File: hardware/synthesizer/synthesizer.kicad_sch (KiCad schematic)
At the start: 23 parts, among them J1 USB_C_Receptacle_USB2.0_14P, J2 Conn_Coaxial, J3 Conn_Coaxial, J4 Conn_Coaxial, J5 Conn_Coaxial, J6 Conn_ARM_JTAG_SWD_10, J7 RJ45_Abracon_ARJP11A-MASA-B-A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, U1 STM32H723VGTx, U2 AP2112K-3.3, U3 USBLC6-2P6

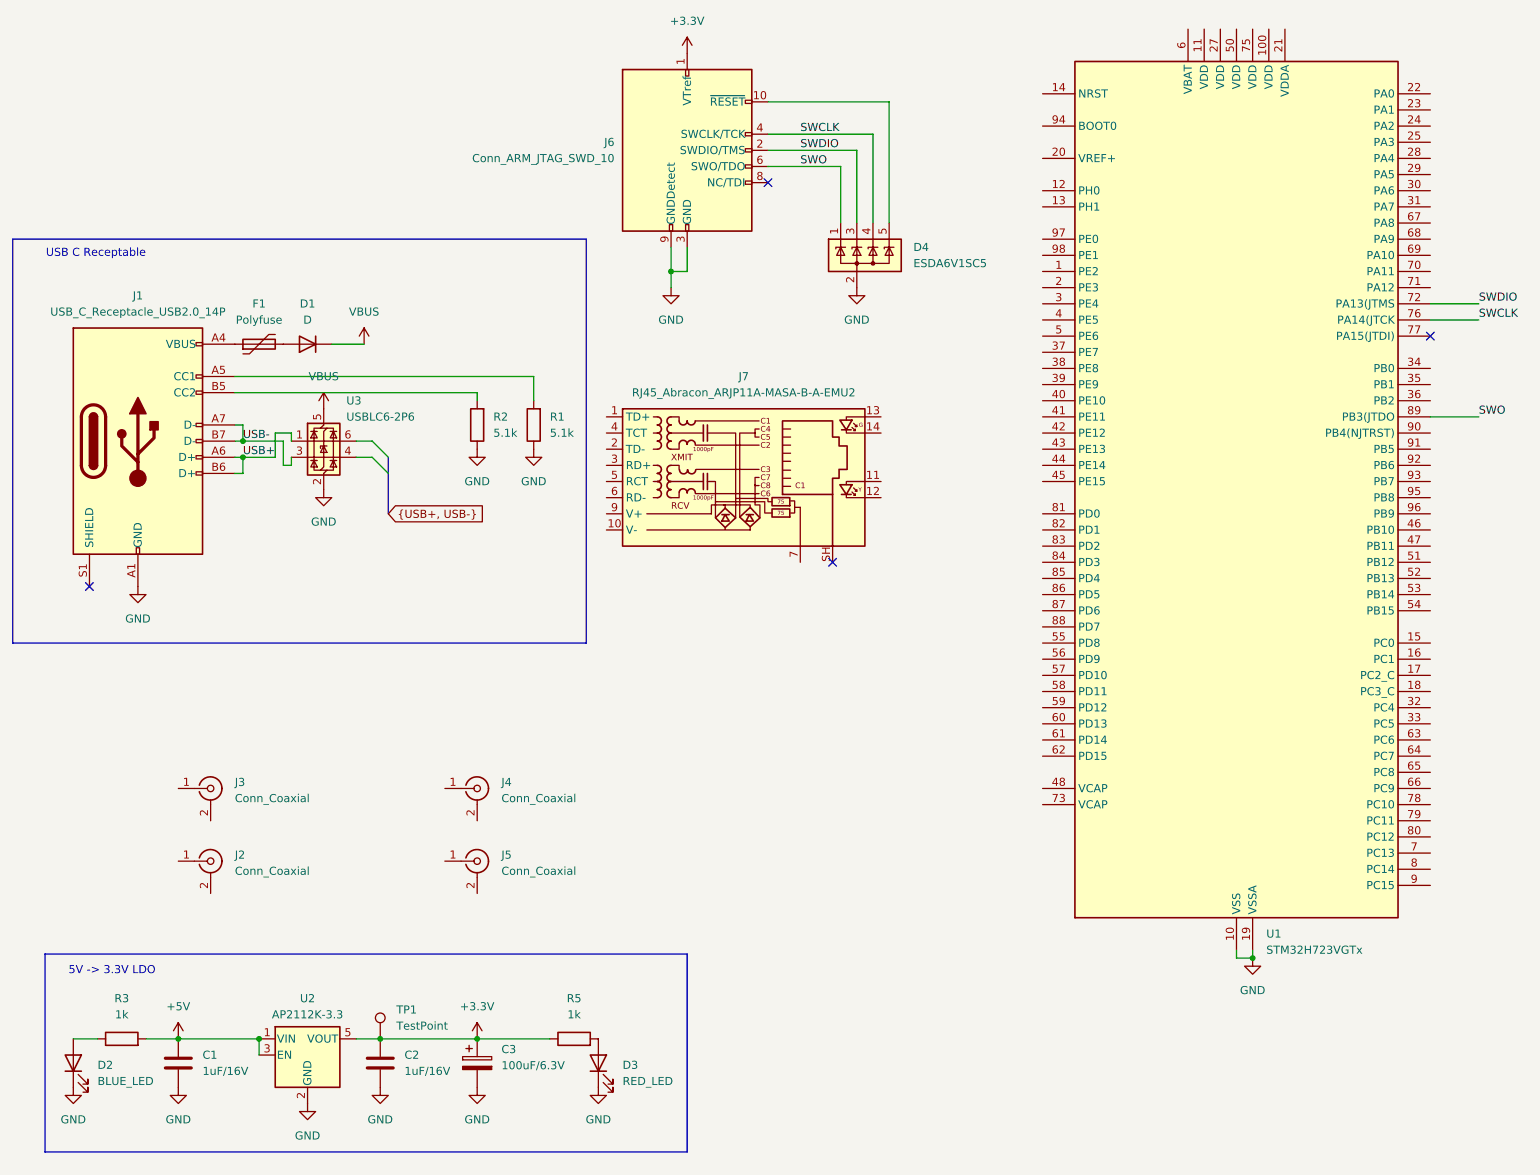
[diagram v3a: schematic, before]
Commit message: created slides for cw8, split schematics
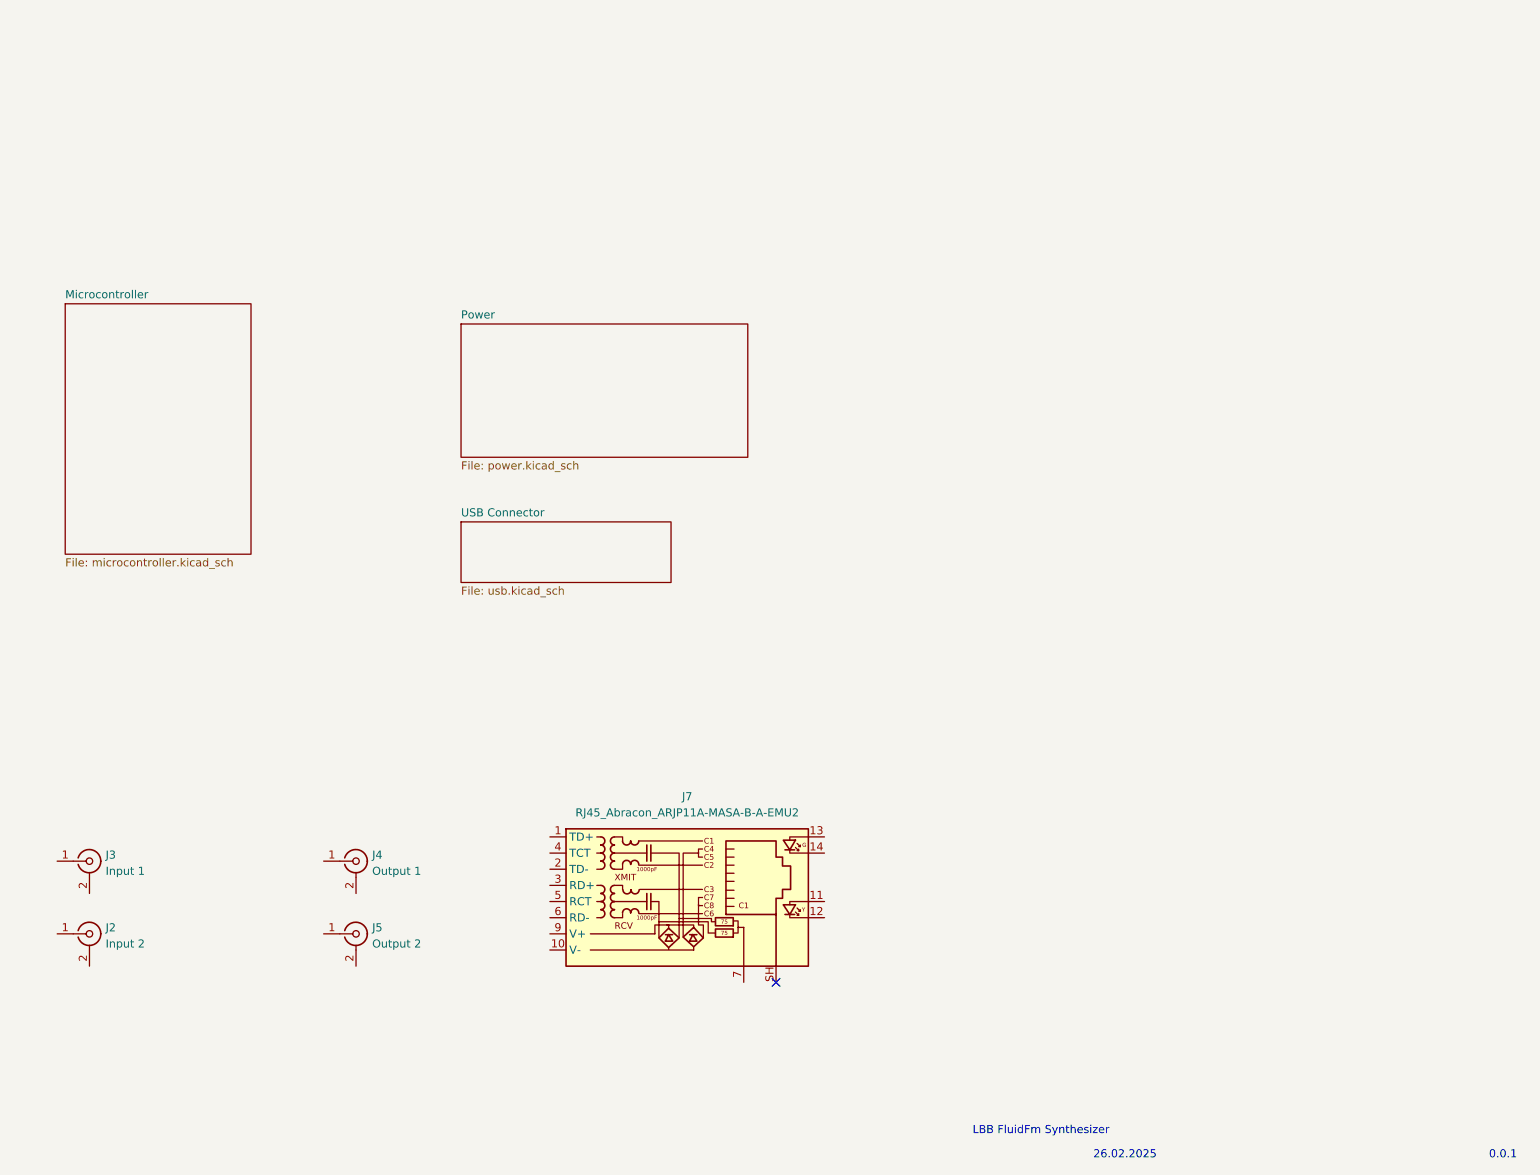
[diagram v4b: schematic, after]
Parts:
- removed C1, C2: 1uF/16V, symbol Device:C
- removed C3: 100uF/6.3V, symbol Device:C_Polarized
- removed D1: D, Diode_SMD:D_0201_0603Metric, symbol Device:D
- removed D2: BLUE_LED, symbol Device:LED
- removed D3: RED_LED, symbol Device:LED
- removed D4: ESDA6V1SC5, Package_TO_SOT_SMD:SOT-23-5, symbol Power_Protection:ESDA6V1SC5
- removed F1: Polyfuse, Fuse:Fuse_Bourns_MF-RG300, symbol Device:Polyfuse
- removed J1: USB_C_Receptacle_USB2.0_14P, symbol Connector:USB_C_Receptacle_USB2.0_14P
- removed J6: Conn_ARM_JTAG_SWD_10, Connector_PinHeader_1.27mm:PinHeader_2x05_P1.27mm_Vertical, symbol Connector:Conn_ARM_JTAG_SWD_10
- removed R1, R2: 5.1k, symbol Device:R
- removed R3, R5: 1k, symbol Device:R
- removed TP1: TestPoint, symbol Connector:TestPoint
- removed U1: STM32H723VGTx, Package_QFP:LQFP-100_14x14mm_P0.5mm, symbol MCU_ST_STM32H7:STM32H723VGTx
- removed U2: AP2112K-3.3, Package_TO_SOT_SMD:SOT-23-5, symbol Regulator_Linear:AP2112K-3.3
- removed U3: USBLC6-2P6, Package_TO_SOT_SMD:SOT-666, symbol Power_Protection:USBLC6-2P6
- J2: value Conn_Coaxial -> Input 2; footprint Connector_Coaxial:SMA_BAT_Wireless_BWSMA-KWE-Z001 -> Connector_Coaxial:BNC_TEConnectivity_1478035_Horizontal
- J3: value Conn_Coaxial -> Input 1; footprint Connector_Coaxial:SMA_BAT_Wireless_BWSMA-KWE-Z001 -> Connector_Coaxial:BNC_TEConnectivity_1478035_Horizontal
- J4: value Conn_Coaxial -> Output 1; footprint Connector_Coaxial:SMA_BAT_Wireless_BWSMA-KWE-Z001 -> Connector_Coaxial:BNC_TEConnectivity_1478035_Horizontal
- J5: value Conn_Coaxial -> Output 2; footprint Connector_Coaxial:SMA_BAT_Wireless_BWSMA-KWE-Z001 -> Connector_Coaxial:BNC_TEConnectivity_1478035_Horizontal
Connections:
- no-connect marks 4 -> 1
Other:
- added sheet Microcontroller (microcontroller.kicad_sch)
- added sheet Power (power.kicad_sch)
- added sheet USB Connector (usb.kicad_sch)
- note added: "0.0.1"
- note added: "26.02.2025"
- note added: "LBB FluidFm Synthesizer"
- note removed: "5V -> 3.3V LDO"
- note removed: "USB C Receptable"
- moved on the sheet: J2, J3, J4, J5, J7

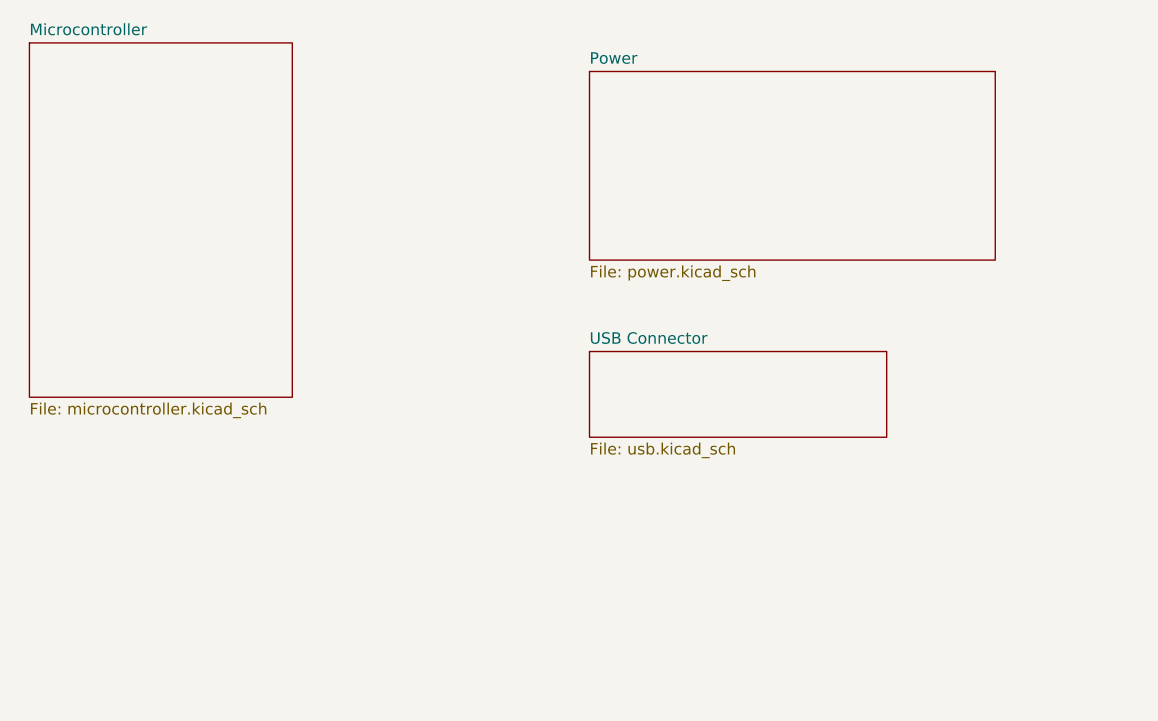
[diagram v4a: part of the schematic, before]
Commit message: start connecting sheets
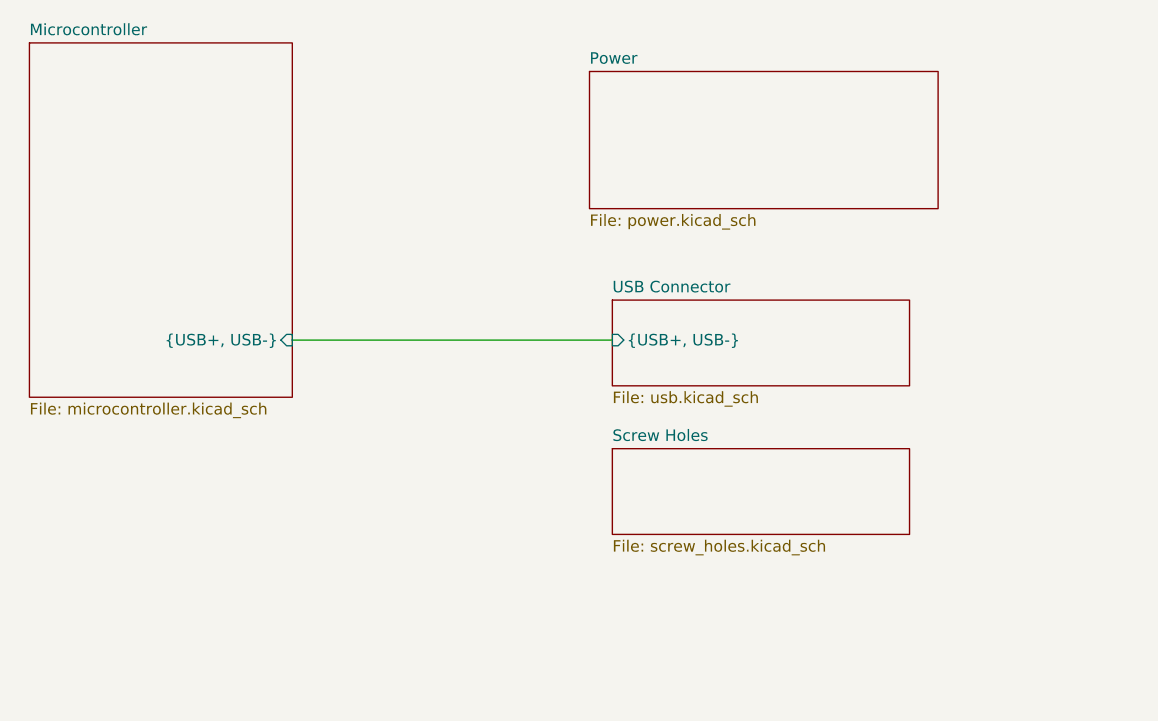
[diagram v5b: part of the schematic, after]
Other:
- added sheet Screw Holes (screw_holes.kicad_sch)
- sheet Microcontroller ports: added {USB+, USB-}; removed none
- sheet USB Connector ports: added {USB+, USB-}; removed none
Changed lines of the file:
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@@
 		(at 157.48 166.37)
+	)
+	(wire
+		(pts
+			(xy 74.93 92.71) (xy 110.49 92.71)
+		)
+		(stroke
+			(width 0)
+			(type default)
+		)
 	)
 	(image
@@
 			"UVBRm1HmUjFSfFLHUxNTX1OqU/ZUQlSPVNtVKFV1VcJWD1ZcVqlW91dEV5JX4FgvWH1Yy1kaWWlZ"
 			"uFoHWlZaplr1W0VblVvlXDVchlzWXSddeF3JXhpebF69Xw9fYV+zYAVgV2CqYPxhT2GiYfViSWKc"
-			"YvBjQ2OXY+tkQGSUZOllPWWSZedmPWaSZuhnPWeTZ+loP2iWaOxpQ2maafFqSGqfag=="
+			"YvBjQ2OXY+tkQGSUZOllPWWSZedmPWaSZuhnPWeTZ+loP2iWaOxpQ2maafFqSGqfagAAAAAAAACQ"
+			"WQkGAgAAAAAAAAAAAAAAAAAAAAAAAAAAAAAAAAAAAAAAAAAAAAAAAAAAAAAAAAAAAAAAAAAAAAAA"
+			"AAAAAAAAAAAAAAAAAAAAAAAAAAAAAAAAAAAAAAAAAAAAAAAAAAAAAAAAAAAAAAAAAAAAAAAAAAAA"
+			"AAAAAAAAAAAAAAAAAAAAAAAAAAAAAAAAAAAAAAAAAAAAAAAAAAAAAAAAAAAAAAAAAAAAAAAAAAAA"
+			"AAAAAAAAAAAAAAAAAAAAAAAAAAAAAAAAAAAAAAAAAAAAAAAAAAAAAAAAAAAAAAAAAAAAAAAAAAAA"
+			"AAAAAAAAAAAAAAAAAAAAAAAAAAAAAAAAAAAAAAAAAAAAAAAAAAAAAAAAAAAAAAAAAAAAAAAAAAAA"
+			"AAAAAAAAAAAAAAAAAAAAAAAAAAAAAAAAAAD/AQAAAAAAAAAEAAAAAAAAAAAAAAAAAAAAAAAAAAAA"
+			"AAAAAAAAAAAAAAAAAAAAAAAAAAAAAAAAAAAAAAAAAAAAAAAAAAAAAAAAAAAAAAAAAAAAAAAAAAAA"
+			"AAAAAAAAAAAAAAAAAAAAAAAAAAAAAAAAAAAAAAAAAAAAAAAAAAAAAAAAAAAAAAAAAAAAAAAAAAAA"
+			"AAAAAAAAAAAAAAAAAAAAAAAAAAAAAAAAAAAAAAAAAAAAAAAAAAAAAAAAAAAAAAAAAAAAAAAAAAAA"
+			"AAAAAAAAAAAAAAAAAAAAAAAAAAAAAAAAAAAAAAAAAAAAAAAAAAAAAAAAAAAAAAAAAAAAAAAAAAAA"
+			"AAAAAAAAAAAAAAAAAAAAAAAAAAAAAAAAAAAAAAAAAAAAAAAAAAAAAAAAAAAAAAAAAAAAAAAAAAAA"
+			"AAAAAAAAAAAAAAAAAAAAAAAAAAAAAAAAAAAAAAAAAAAAAAAAAAAAAAAAAAAAAAAAAAAAAAAAAAAA"
+			"AAAAAAAAAAAAAAAAAAAAAAAAAAAAAAAAAAAAAAAAAAAAAAAAAAAAAAAAAAAAAAAAAAAAAAAAAAAA"
+			"AAAAAAAAAAAAAAAAAAAAAAAAAAAAAAAAAAAAAAAAAAAAAAAAAAAAAAAAAAAAAAAAAAAAAAAAAAAA"
+			"AAAAAAAAAAAAAAAAAAAAAAAAAAAAAAAAAAAAAAAAAAAAAAAAAAAAAAAAAAAAAAAAAAAAAAAAAAAA"
+			"AAAAAAAAAAAAAAAAAAAAAAAAAAAAAAAAAAAAAAAAAAAAAAAAAAAAAAAAAAAAAAAAAAAAAAAAAAAA"
+			"AAAAAAAAAAAAAAAAAAAAAAAAAAAAAAAAAAAAAAAAAAAAAAAAAAAAAAAAAAAAAAAAAAAAAAAAAAAA"
+			"AAAAAAAAAAAAAAAAAAAAAAAAAAAAAAAAAAAAAAAAAAAAAAAAAAAAAAAAAAAAAAAAAA=="
 		)
 	)
@@
 			"AAAAAAAAAAAAAAAAAAAAAAAAAAAAAAAAAAAAAAAAAAAAAAAAAAAAAAAAAAAAAAAAAAAAAAAAAAAA"
 			"AAAAAAAAAAAAAAAAAAAAAAAAAAAAAAAAAAAAAAAAAAAAAAAAAAAAAAAAAAAAAAAAAAAAAAAAAAAA"
+			"AAAAAAAAAAAAAAAAAAAAAAAAAAAAAAAAAAAAAAAAAAAAAAAAAAAAAAAAAAAAAAAAAAAAAAAAAAAA"
+			"AAAAAAAAAAAAAAAAAAAAAAAAAAAAAAAAAAAAAAAAAAAAAAAAAAAAAAAAAAAAAAAAAAAAAAAAAAAA"
+			"AAAAAAAAAAAAAAAAAAAAAAAAAAAAAAAAAAAAAAAAAAAAAAAAAAAAAAAAAAAAAAAAAAAAAAAAAAAA"
+			"AAAAAAAAAAAAAAAAAAAAAAAAAAAAAAAAAAAAAAAAAAAAAAAAAAAAAAAAAAAAAAAAAAAAAAAAAAAA"
+			"AAAAAAAAAAAAAAAAAAAAAAAAAAAAAAAAAAAAAAAAAAAAAAAAAAAAAAAAAAAAAAAAAAAAAAAAAAAA"
+			"AAAAAAAAAAAAAAAAAAAAAAAAAAAAAAAAAAAAAAAAAAAAAAAAAAAAAAAAAAAAAAAAAAAAAAAAAAAA"
+			"AAAAAAAAAAAAAAAAAAAAAAAAAAAAAAAAAAAAAAAAAAAAAAAAAAAAAAAAAAAAAAAAAAAAAAAAAAAA"
+			"AAAAAAAAAAAAAAAAAAAAAAAAAAAAAAAAAAAAAAAAAAAAAAAAAAAAAAAAAAAAAAAAAAAAAAAAAAAA"
+			"AAAAAAAAAAAAAAAAAAAAAAAAAAAAAAAAAAAAAAAAAAAAAAAAAAAAAAAAAAAAAAAAAAAAAAAAAAAA"
+			"AAAAAAAAAAAAAAAAAAAAAAAAAAAAAAAAAAAAAAAAAAAAAAAAAAAAAAAAAAAAAAAAAAAAAAAAAAAA"
+			"AAAAAAAAAAAAAAAAAAAAAAAAAAAAAAAAAAAAAAAAAAAAAAAAAAAAAAAAAAAAAAAAAAAAAAAAAAAA"
+			"AAAAAAAAAAAAAAAAAAAAAAAAAAAAAAAAAAAAAAAAAAAAAAAAAAAAAAAAAAAAAAAAAAAAAAAAAAAA"
+			"AAAAAAAAAAAAAAAAAAAAAAAAAAAAAAAAAAAAAAAAAAAAAAAAAAAAAAAAAAAAAAAAAAAAAAAAAAAA"
+			"AAAAAAAAAAAAAAAAAAAAAAAAAAAAAAAAAAAAAAAAAAAAAAAAAAAAAAAAAAAAAAAAAAAAAAAAAAAA"
+			"AAAAAAAAAAAAAAAAAAAAAAAAAAAAAAAAAAAAAAAAAAAAAAAAAAAAAAAAAAAAAAAAAAAAAAAAAAAA"
+			"AAAAAAAAAAAAAAAAAAAAAAAAAAAAAAAAAAAAAAAAAAAAAAAAAAAAAAAAAAAAAAAAAAAAAAAAAAAA"
+			"AAAAAAAAAAAAAAAAAAAAAAAAAAAAAAAAAAAAAAAAAAAAAAAAAAAAAAAAAAAAAAAAAAAAAAAAAAAA"
+			"AAAAAAAAAAAAAAAAAAAAAAAAAAAAAAAAAAAAAAAAAAAAAAAAAAAAAAAAAAAAAAAAAAAAAAAAAAAA"
 			"AAAAAAAAAA=="
 		)
@@
 	)
 	(sheet
-		(at 107.95 93.98)
+		(at 110.49 88.265)
 		(size 33.02 9.525)
 		(exclude_from_sim no)
@@
 		)
 		(property "Sheetname" "USB Connector"
-			(at 107.95 93.2684 0)
+			(at 110.49 87.5534 0)
 			(effects
 				(font
@@
 		)
 		(property "Sheetfile" "usb.kicad_sch"
-			(at 107.95 104.0896 0)
+			(at 110.49 98.3746 0)
 			(effects
 				(font
@@
 				)
 				(justify left top)
+			)
+		)
+		(pin "{USB+, USB-}" input
+			(at 110.49 92.71 180)
+			(effects
+				(font
+					(size 1.27 1.27)
+				)
+				(justify left)
 			)
 		)
@@
 	(sheet
 		(at 107.95 62.865)
-		(size 45.085 20.955)
+		(size 38.735 15.24)
 		(exclude_from_sim no)
 		(in_bom yes)
@@
 		)
 		(property "Sheetfile" "power.kicad_sch"
-			(at 107.95 84.4046 0)
+			(at 107.95 78.6896 0)
 			(effects
 				(font
@@
 				(path "/f8740766-88d0-4c4d-b661-742f36f22c7b"
 					(page "3")
+				)
+			)
+		)
+	)
+	(sheet
+		(at 110.49 104.775)
+		(size 33.02 9.525)
+		(exclude_from_sim no)
+		(in_bom yes)
+		(on_board yes)
+		(dnp no)
+		(fields_autoplaced yes)
+		(stroke
+			(width 0.1524)
+			(type solid)
+		)
+		(fill
+			(color 200 252 188 1.0000)
+		)
+		(property "Sheetname" "Screw Holes"
+			(at 110.49 104.0634 0)
+			(effects
+				(font
+					(size 1.27 1.27)
+				)
+				(justify left bottom)
+			)
+		)
+		(property "Sheetfile" "screw_holes.kicad_sch"
+			(at 110.49 114.8846 0)
+			(effects
+				(font
+					(size 1.27 1.27)
+				)
+				(justify left top)
+			)
+		)
+		(instances
+			(project "synthesizer"
+				(path "/f8740766-88d0-4c4d-b661-742f36f22c7b"
+					(page "5")
 				)
 			)
@@
 			)
 		)
+		(pin "{USB+, USB-}" input
+			(at 74.93 92.71 0)
+			(effects
+				(font
+					(size 1.27 1.27)
+				)
+				(justify right)
+			)
+		)
